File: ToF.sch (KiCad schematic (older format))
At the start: 1 part, among them J5 Conn_01x05

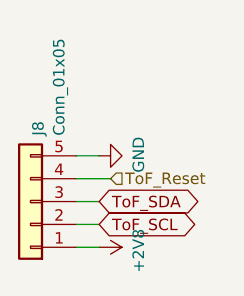
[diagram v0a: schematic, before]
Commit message: PCB routed, no errors but still a few tracks too close
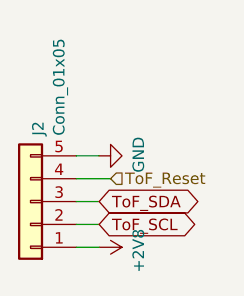
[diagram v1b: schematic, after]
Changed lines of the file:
@@
 AR Path="/5BBFB811/5BBF8577" Ref="J8"  Part="1"
 AR Path="/5BBFB816/5BBF8577" Ref="J9"  Part="1"
-F 0 "J8" V 3216 3312 50  0000 R CNN
+F 0 "J2" V 3216 3312 50  0000 R CNN
 F 1 "Conn_01x05" V 3125 3312 50  0000 R CNN
 F 2 "Connector_JST:JST_PH_B5B-PH-K_1x05_P2.00mm_Vertical" H 3250 3600 50  0001 C CNN
@@
 AR Path="/5BBFB811/5BBF857E" Ref="#PWR048"  Part="1"
 AR Path="/5BBFB816/5BBF857E" Ref="#PWR050"  Part="1"
-F 0 "#PWR048" H 3550 3650 50  0001 C CNN
+F 0 "#PWR036" H 3550 3650 50  0001 C CNN
 F 1 "+2V8" H 3565 3973 50  0000 C CNN
 F 2 "" H 3550 3800 50  0001 C CNN
@@
 AR Path="/5BBFB811/5BBF8585" Ref="#PWR047"  Part="1"
 AR Path="/5BBFB816/5BBF8585" Ref="#PWR049"  Part="1"
-F 0 "#PWR047" H 3550 3150 50  0001 C CNN
+F 0 "#PWR035" H 3550 3150 50  0001 C CNN
 F 1 "GND" H 3555 3227 50  0000 C CNN
 F 2 "" H 3550 3400 50  0001 C CNN
